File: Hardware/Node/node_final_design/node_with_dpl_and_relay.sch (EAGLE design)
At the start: 58 parts, among them K1 G6RS, T1 FDN340P, U1 NCP1117ST50T3G, U2 LP2985-33DBVR, U5 LMV358IDGKR, X1 POWERSUPPLY_DC21MMX, Y1 8Mhz, Y2 CSTCE16M0V53-R0 16MHZ

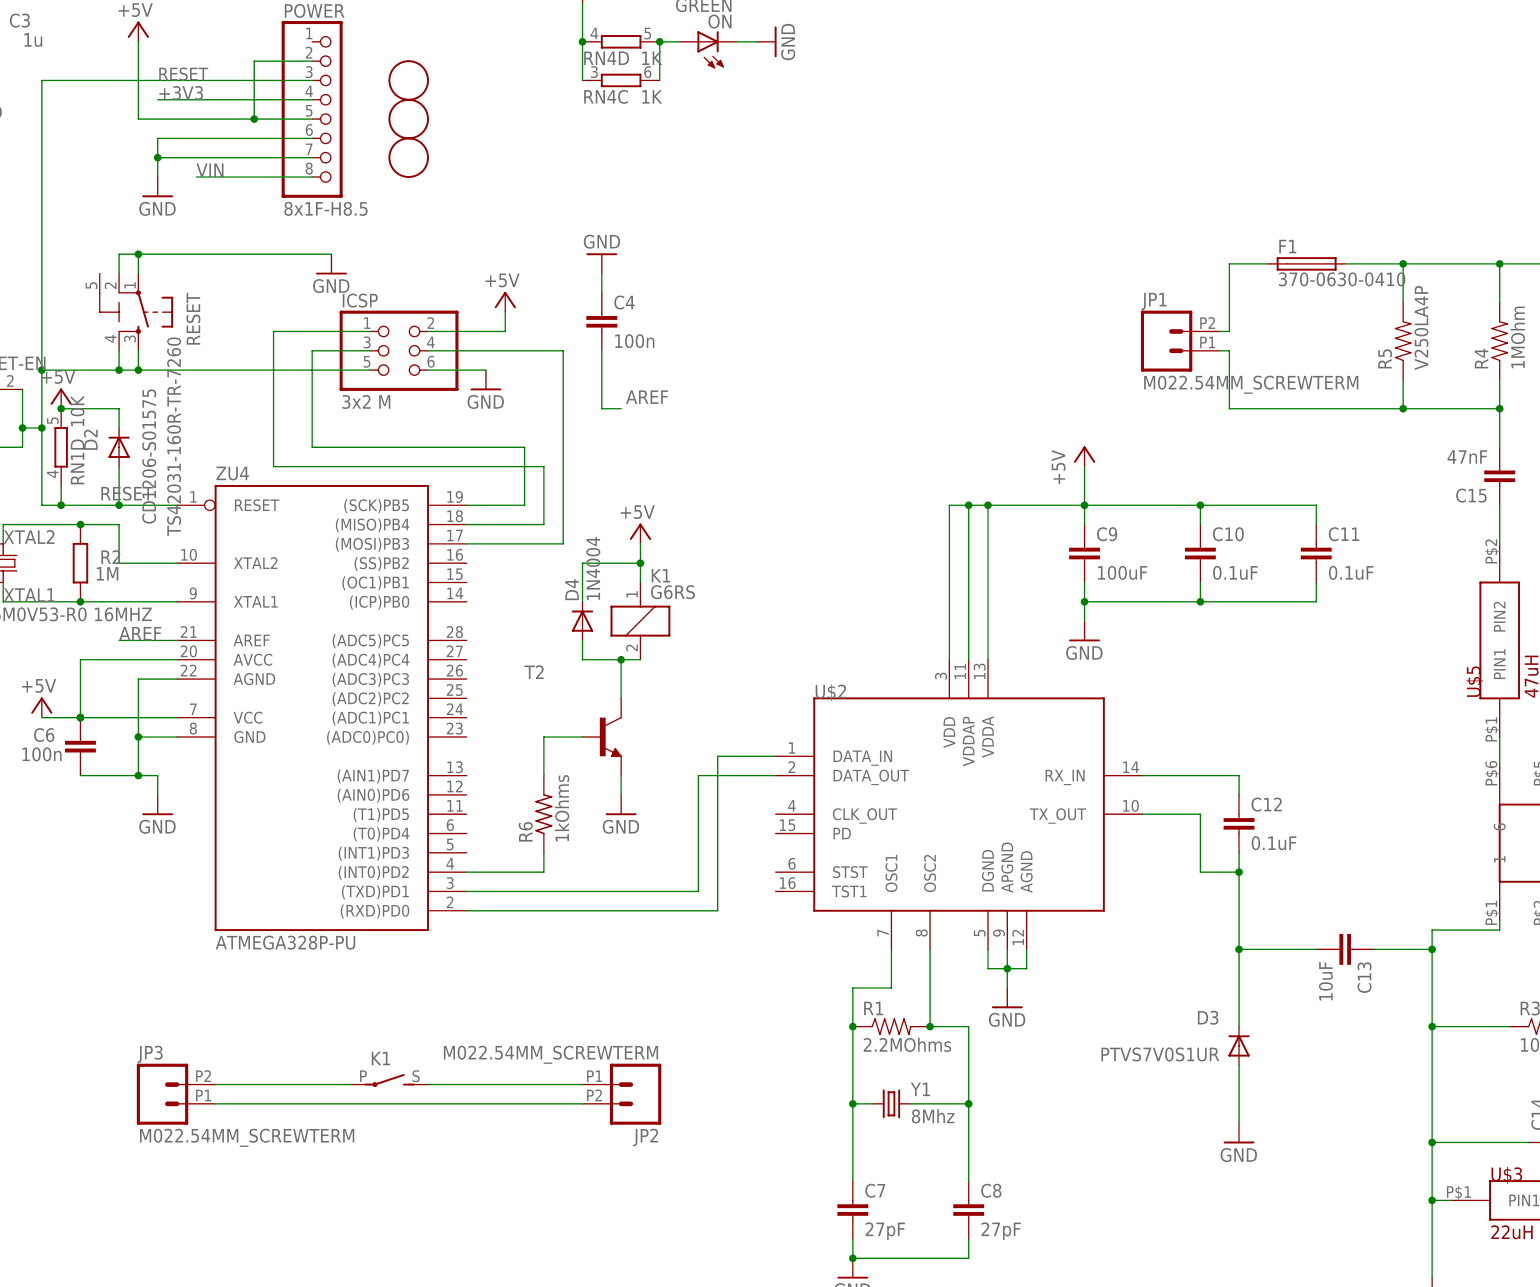
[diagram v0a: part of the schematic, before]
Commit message: Started node pcb layout
not finished yet
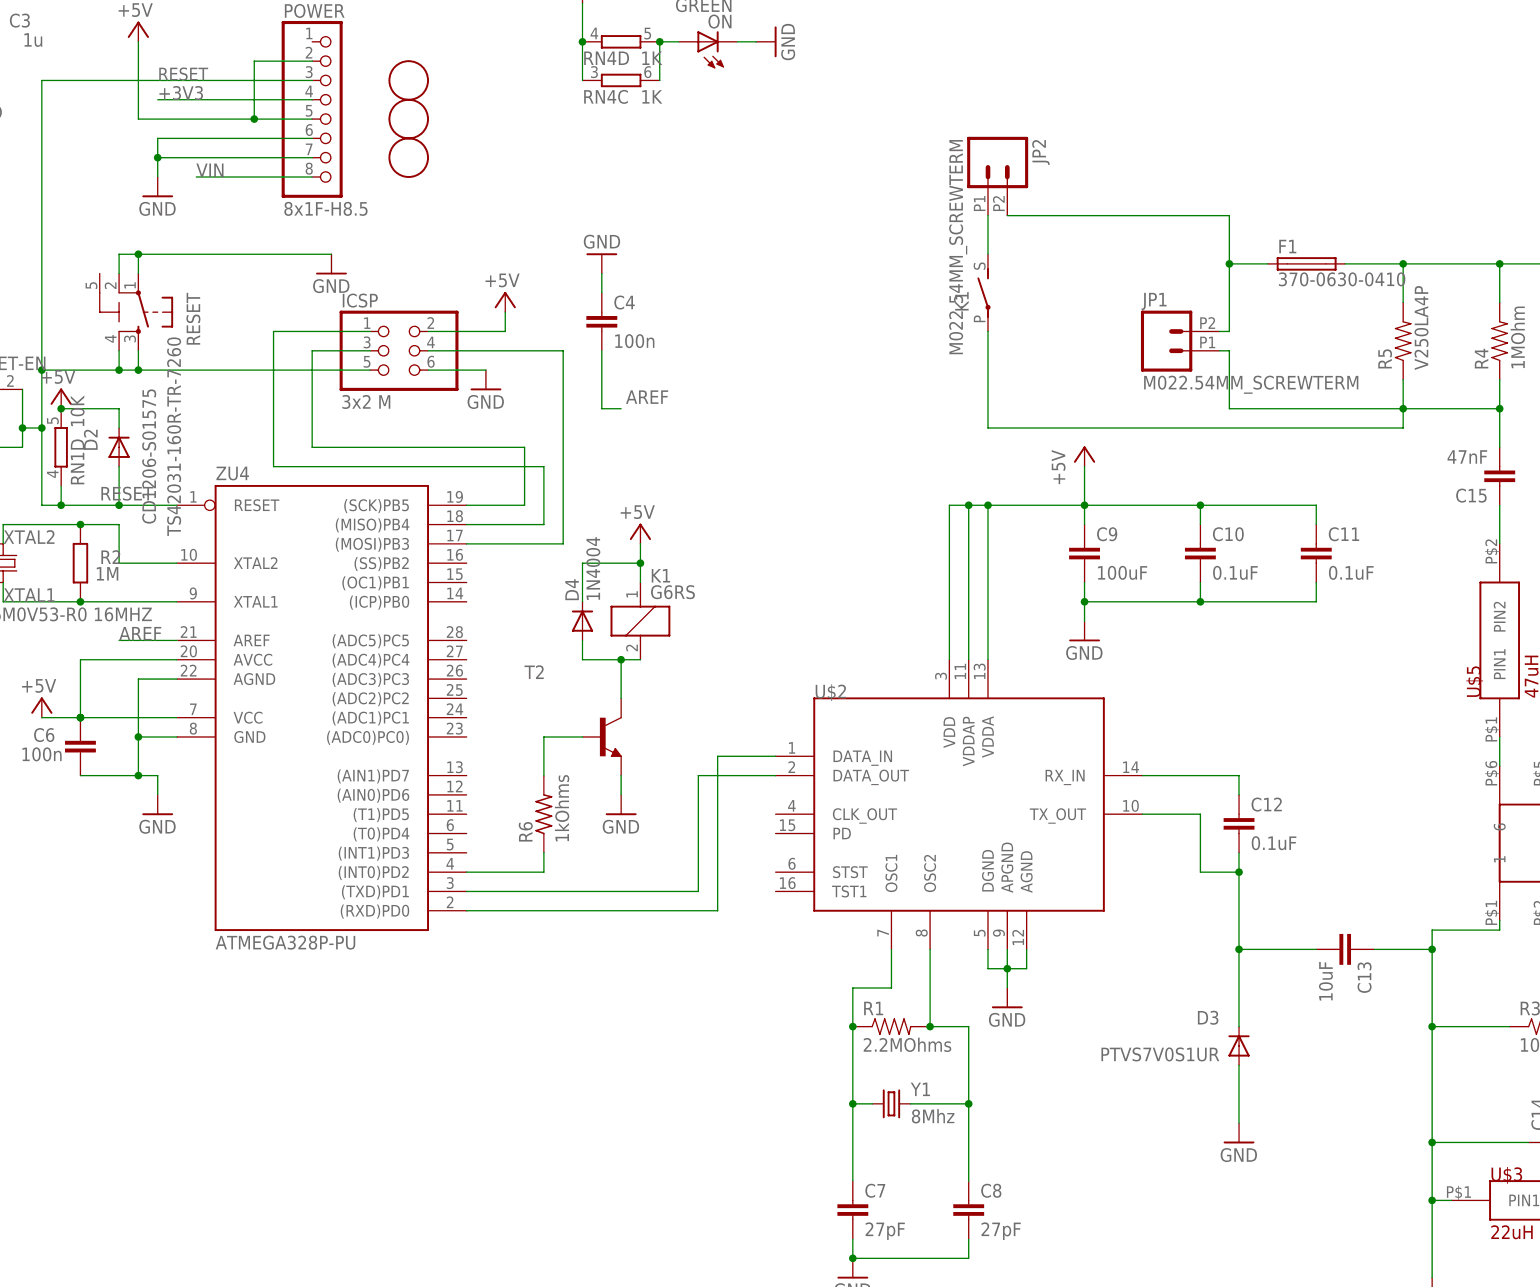
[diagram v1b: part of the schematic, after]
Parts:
- removed JP3: M022.54MM_SCREWTERM, SparkFun-Connectors:M022.54MM_SCREWTERM
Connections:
- removed net N$11 (its old number): C15.2, JP1.1, R4.1, R5.1
- removed net N$18: JP3.2, K12.P
- net N$12: now also JP2.2
- net N$19: now also C15.2, JP1.1, K12.P, R4.1, R5.1; no longer JP2.2, JP3.1
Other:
- moved on the sheet: JP2, K1

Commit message: node pcb done
should work
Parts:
- removed FD1, FD2, FD3: FIDUCIALMOUNT, SmartPrj:FIDUCIALMOUNT
- removed RN3: 22R, resistor-dil:4R-NCAY16
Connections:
- net GND: now also RESET.5-GND
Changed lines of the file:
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@@
 <part name="D1" library="diode" deviceset="DIODE-" device="SMB" value="M7"/>
 <part name="X1" library="SmartPrj" deviceset="POWERSUPPLY_DC21MM" device="X"/>
-<part name="FD1" library="SmartPrj" deviceset="FIDUCIALMOUNT" device=""/>
-<part name="FD2" library="SmartPrj" deviceset="FIDUCIALMOUNT" device=""/>
-<part name="FD3" library="SmartPrj" deviceset="FIDUCIALMOUNT" device=""/>
 <part name="GND11" library="supply1" deviceset="GND" device=""/>
 <part name="U1" library="linear" deviceset="MC33269ST*" device="" technology="-3.3T3" value="NCP1117ST50T3G"/>
@@
 <part name="C6" library="SmartPrj" deviceset="C-EU" device="0603-RND" value="100n"/>
 <part name="RN4" library="resistor-dil" deviceset="4R-N" device="CAY16" value="1K"/>
-<part name="RN3" library="resistor-dil" deviceset="4R-N" device="CAY16" value="22R"/>
 <part name="C3" library="SmartPrj" deviceset="C-EU" device="0603-RND" value="1u"/>
 <part name="GND15" library="supply1" deviceset="GND" device=""/>
@@
 <attribute name="VALUE" x="116.84" y="182.88" size="1.27" layer="94"/>
 </instance>
-<instance part="FD1" gate="G$1" x="167.64" y="134.62"/>
-<instance part="FD2" gate="G$1" x="167.64" y="129.54"/>
-<instance part="FD3" gate="G$1" x="167.64" y="124.46"/>
 <instance part="GND11" gate="1" x="180.34" y="157.48"/>
 <instance part="U1" gate="G$1" x="180.34" y="172.72" smashed="yes">
@@
 <instance part="RN4" gate="C" x="195.58" y="134.62"/>
 <instance part="RN4" gate="D" x="195.58" y="139.7"/>
-<instance part="RN3" gate="B" x="233.68" y="-33.02"/>
-<instance part="RN3" gate="C" x="233.68" y="-40.64"/>
 <instance part="C3" gate="G$1" x="111.76" y="139.7" smashed="yes" rot="MR180">
 <attribute name="NAME" x="117.983" y="141.605" size="1.778" layer="95" rot="MR0"/>
@@
 <pinref part="RESET" gate="G$1" pin="2"/>
 <pinref part="RESET" gate="G$1" pin="1"/>
-</segment>
-<segment>
+<pinref part="RESET" gate="G$1" pin="5-GND"/>
+<wire x1="129.54" y1="111.76" x2="127" y2="111.76" width="0.1524" layer="91"/>
+<wire x1="127" y1="111.76" x2="127" y2="109.22" width="0.1524" layer="91"/>
+<junction x="129.54" y="111.76"/>
+</segment>
+<segment>
